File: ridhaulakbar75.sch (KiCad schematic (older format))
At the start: 184 parts, among them J1 SWD, J2 Ex_Bat, J3 Ex_USB, J4 RESET, J5 Underglow, Q1 AO3407, Q2 AO3407, SW1 Rotary_Encoder_Switch, U2 E73-2G4M08S1C-52840, U3 XC6220B331MR, U4 TP4054, Y1 32.768kHz

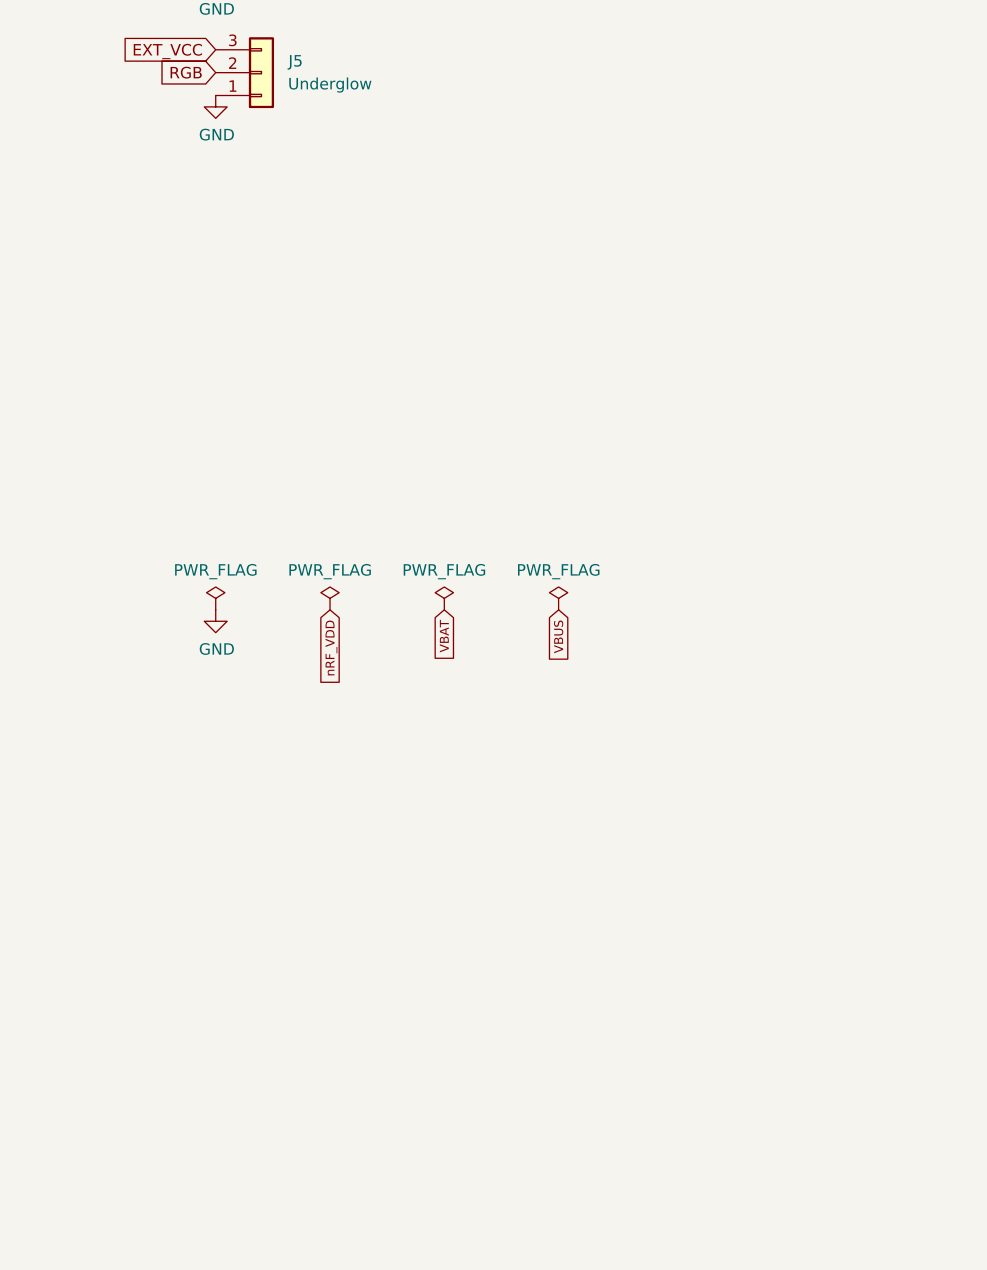
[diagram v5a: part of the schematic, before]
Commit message: add usb c back and add iso
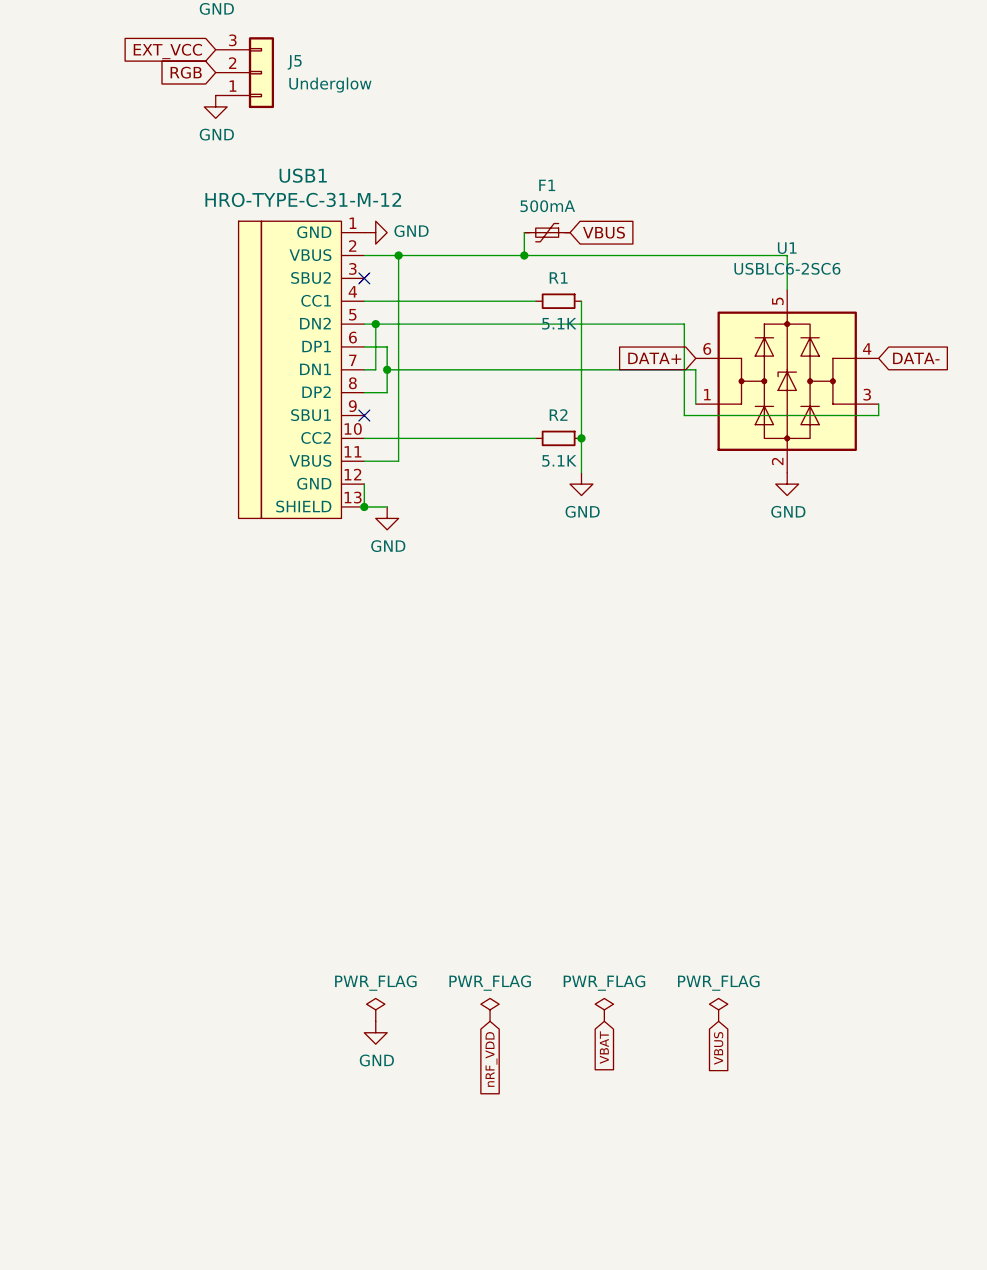
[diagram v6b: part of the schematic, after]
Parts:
- added F1: 500mA, Fuse:Fuse_1206_3216Metric, symbol Device:Polyfuse_Small
- added R1, R2: 5.1K, Resistor_SMD:R_0603_1608Metric, symbol Device:R_Small
- added U1: USBLC6-2SC6, Package_TO_SOT_SMD:SOT-23-6, symbol Power_Protection:USBLC6-2SC6
- added USB1: HRO-TYPE-C-31-M-12, Type-C:HRO-TYPE-C-31-M-12-HandSoldering, symbol keebio:HRO-TYPE-C-31-M-12
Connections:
- net DATA+: now also U1.6 (I/O1)
- net DATA-: now also U1.4 (I/O2)
- net GND: now also R1.1, R2.1, U1.2 (GND), USB1.1 (GND), USB1.12 (GND), USB1.13 (SHIELD)
- net VBUS: now also F1.1
- new net: R2.2, USB1.10 (CC2)
- new net: F1.2, U1.5 (VBUS), USB1.11 (VBUS), USB1.2 (VBUS)
- new net: R1.2, USB1.4 (CC1)
- new net: U1.3 (I/O2), USB1.5 (DN2), USB1.7 (DN1)
- new net: U1.1 (I/O1), USB1.6 (DP1), USB1.8 (DP2)
- no-connect marks 0 -> 2
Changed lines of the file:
@@
 L power:PWR_FLAG #FLG01
 U 1 1 60D8BBF8
-P 11250 7800
-F 0 "#FLG01" H 11250 7875 50  0001 C CNN
-F 1 "PWR_FLAG" H 11250 7973 50  0000 C CNN
-F 2 "" H 11250 7800 50  0001 C CNN
-F 3 "~" H 11250 7800 50  0001 C CNN
-	1    11250 7800
+P 11950 9600
+F 0 "#FLG01" H 11950 9675 50  0001 C CNN
+F 1 "PWR_FLAG" H 11950 9773 50  0000 C CNN
+F 2 "" H 11950 9600 50  0001 C CNN
+F 3 "~" H 11950 9600 50  0001 C CNN
+	1    11950 9600
 	1    0    0    -1
 $EndComp
@@
 L power:PWR_FLAG #FLG02
 U 1 1 60D8D705
-P 11750 7800
-F 0 "#FLG02" H 11750 7875 50  0001 C CNN
-F 1 "PWR_FLAG" H 11750 7973 50  0000 C CNN
-F 2 "" H 11750 7800 50  0001 C CNN
-F 3 "~" H 11750 7800 50  0001 C CNN
-	1    11750 7800
+P 12450 9600
+F 0 "#FLG02" H 12450 9675 50  0001 C CNN
+F 1 "PWR_FLAG" H 12450 9773 50  0000 C CNN
+F 2 "" H 12450 9600 50  0001 C CNN
+F 3 "~" H 12450 9600 50  0001 C CNN
+	1    12450 9600
 	1    0    0    -1
 $EndComp
@@
 L power:PWR_FLAG #FLG03
 U 1 1 60D8DA8A
-P 12250 7800
-F 0 "#FLG03" H 12250 7875 50  0001 C CNN
-F 1 "PWR_FLAG" H 12250 7973 50  0000 C CNN
-F 2 "" H 12250 7800 50  0001 C CNN
-F 3 "~" H 12250 7800 50  0001 C CNN
-	1    12250 7800
+P 12950 9600
+F 0 "#FLG03" H 12950 9675 50  0001 C CNN
+F 1 "PWR_FLAG" H 12950 9773 50  0000 C CNN
+F 2 "" H 12950 9600 50  0001 C CNN
+F 3 "~" H 12950 9600 50  0001 C CNN
+	1    12950 9600
 	1    0    0    -1
 $EndComp
@@
 L power:PWR_FLAG #FLG04
 U 1 1 60D8DE71
-P 12750 7800
-F 0 "#FLG04" H 12750 7875 50  0001 C CNN
-F 1 "PWR_FLAG" H 12750 7973 50  0000 C CNN
-F 2 "" H 12750 7800 50  0001 C CNN
-F 3 "~" H 12750 7800 50  0001 C CNN
-	1    12750 7800
+P 13450 9600
+F 0 "#FLG04" H 13450 9675 50  0001 C CNN
+F 1 "PWR_FLAG" H 13450 9773 50  0000 C CNN
+F 2 "" H 13450 9600 50  0001 C CNN
+F 3 "~" H 13450 9600 50  0001 C CNN
+	1    13450 9600
 	1    0    0    -1
 $EndComp
@@
 L power:GND #PWR07
 U 1 1 60D8F3D0
-P 11250 7800
-F 0 "#PWR07" H 11250 7550 50  0001 C CNN
-F 1 "GND" H 11255 7627 50  0000 C CNN
-F 2 "" H 11250 7800 50  0001 C CNN
-F 3 "" H 11250 7800 50  0001 C CNN
-	1    11250 7800
-	1    0    0    -1
-$EndComp
-Text GLabel 11750 7800 3    39   Input ~ 0
+P 11950 9600
+F 0 "#PWR07" H 11950 9350 50  0001 C CNN
+F 1 "GND" H 11955 9427 50  0000 C CNN
+F 2 "" H 11950 9600 50  0001 C CNN
+F 3 "" H 11950 9600 50  0001 C CNN
+	1    11950 9600
+	1    0    0    -1
+$EndComp
+Text GLabel 12450 9600 3    39   Input ~ 0
 nRF_VDD
-Text GLabel 12250 7800 3    39   Input ~ 0
+Text GLabel 12950 9600 3    39   Input ~ 0
 VBAT
-Text GLabel 12750 7800 3    39   Input ~ 0
+Text GLabel 13450 9600 3    39   Input ~ 0
 VBUS
 $Comp
@@
 Text GLabel 11250 5350 0    50   Input ~ 0
 EXT_VCC
+$Comp
+L keebio:HRO-TYPE-C-31-M-12 USB1
+U 1 1 605D3C2A
+P 11800 6700
+F 0 "USB1" H 11633 7497 60  0000 C CNN
+F 1 "HRO-TYPE-C-31-M-12" H 11633 7391 60  0000 C CNN
+F 2 "Type-C:HRO-TYPE-C-31-M-12-HandSoldering" H 11800 6700 60  0001 C CNN
+F 3 "" H 11800 6700 60  0001 C CNN
+	1    11800 6700
+	1    0    0    -1
+$EndComp
+$Comp
+L Device:Polyfuse_Small F1
+U 1 1 605D8FD4
+P 12700 6150
+F 0 "F1" V 12495 6150 50  0000 C CNN
+F 1 "500mA" V 12586 6150 50  0000 C CNN
+F 2 "Fuse:Fuse_1206_3216Metric" H 12750 5950 50  0001 L CNN
+F 3 "~" H 12700 6150 50  0001 C CNN
+	1    12700 6150
+	0    1    1    0
+$EndComp
+$Comp
+L Power_Protection:USBLC6-2SC6 U1
+U 1 1 605DD6E7
+P 13750 6800
+F 0 "U1" H 13750 7381 50  0000 C CNN
+F 1 "USBLC6-2SC6" H 13750 7290 50  0000 C CNN
+F 2 "Package_TO_SOT_SMD:SOT-23-6" H 13750 6300 50  0001 C CNN
+F 3 "https://www.st.com/resource/en/datasheet/usblc6-2.pdf" H 13950 7150 50  0001 C CNN
+	1    13750 6800
+	1    0    0    -1
+$EndComp
+$Comp
+L Device:R_Small R1
+U 1 1 605DED28
+P 12750 6450
+F 0 "R1" V 12650 6450 50  0000 C CNN
+F 1 "5.1K" V 12850 6450 50  0000 C CNN
+F 2 "Resistor_SMD:R_0603_1608Metric" H 12750 6450 50  0001 C CNN
+F 3 "~" H 12750 6450 50  0001 C CNN
+	1    12750 6450
+	0    1    1    0
+$EndComp
+NoConn ~ 11900 6950
+NoConn ~ 11900 6350
+Wire Wire Line
+	11900 7250 11900 7350
+Wire Wire Line
+	11900 7350 12000 7350
+Connection ~ 11900 7350
+$Comp
+L power:GND #PWR0103
+U 1 1 60636907
+P 12000 7350
+F 0 "#PWR0103" H 12000 7100 50  0001 C CNN
+F 1 "GND" H 12005 7177 50  0000 C CNN
+F 2 "" H 12000 7350 50  0001 C CNN
+F 3 "" H 12000 7350 50  0001 C CNN
+	1    12000 7350
+	1    0    0    -1
+$EndComp
+$Comp
+L power:GND #PWR0104
+U 1 1 60639607
+P 11900 6150
+F 0 "#PWR0104" H 11900 5900 50  0001 C CNN
+F 1 "GND" V 11905 6022 50  0000 R CNN
+F 2 "" H 11900 6150 50  0001 C CNN
+F 3 "" H 11900 6150 50  0001 C CNN
+	1    11900 6150
+	0    -1   -1   0
+$EndComp
+Wire Wire Line
+	13750 6250 13750 6400
+Wire Wire Line
+	12600 6250 13750 6250
+Text GLabel 12800 6150 2    50   Input ~ 0
+VBUS
+Wire Wire Line
+	12600 6150 12600 6250
+Wire Wire Line
+	11900 6250 12050 6250
+Connection ~ 12600 6250
+$Comp
+L Device:R_Small R2
+U 1 1 60678896
+P 12750 7050
+F 0 "R2" V 12650 7050 50  0000 C CNN
+F 1 "5.1K" V 12850 7050 50  0000 C CNN
+F 2 "Resistor_SMD:R_0603_1608Metric" H 12750 7050 50  0001 C CNN
+F 3 "~" H 12750 7050 50  0001 C CNN
+	1    12750 7050
+	0    1    1    0
+$EndComp
+Wire Wire Line
+	11900 6450 12650 6450
+Wire Wire Line
+	11900 7050 12650 7050
+Wire Wire Line
+	12850 6450 12850 7050
+Connection ~ 12850 7050
+Wire Wire Line
+	12850 7050 12850 7200
+$Comp
+L power:GND #PWR0105
+U 1 1 606CF4F1
+P 12850 7200
+F 0 "#PWR0105" H 12850 6950 50  0001 C CNN
+F 1 "GND" H 12855 7027 50  0000 C CNN
+F 2 "" H 12850 7200 50  0001 C CNN
+F 3 "" H 12850 7200 50  0001 C CNN
+	1    12850 7200
+	1    0    0    -1
+$EndComp
+Wire Wire Line
+	11900 6550 11950 6550
+Wire Wire Line
+	11950 6550 11950 6750
+Wire Wire Line
+	11950 6750 11900 6750
+Wire Wire Line
+	11900 6650 12000 6650
+Wire Wire Line
+	12000 6650 12000 6750
+Wire Wire Line
+	12000 6850 11900 6850
+Wire Wire Line
+	11900 7150 12050 7150
+Wire Wire Line
+	12050 7150 12050 6250
+Connection ~ 12050 6250
+Wire Wire Line
+	12050 6250 12600 6250
+$Comp
+L power:GND #PWR0106
+U 1 1 60727314
+P 13750 7200
+F 0 "#PWR0106" H 13750 6950 50  0001 C CNN
+F 1 "GND" H 13755 7027 50  0000 C CNN
+F 2 "" H 13750 7200 50  0001 C CNN
+F 3 "" H 13750 7200 50  0001 C CNN
+	1    13750 7200
+	1    0    0    -1
+$EndComp
+Wire Wire Line
+	12000 6750 13350 6750
+Wire Wire Line
+	13350 6750 13350 6900
+Connection ~ 12000 6750
+Wire Wire Line
+	12000 6750 12000 6850
+Wire Wire Line
+	11950 6550 13300 6550
+Wire Wire Line
+	13300 6550 13300 6950
+Wire Wire Line
+	13300 6950 14150 6950
+Wire Wire Line
+	14150 6950 14150 6900
+Connection ~ 11950 6550
+Text GLabel 14150 6700 2    50   Input ~ 0
+DATA-
+Text GLabel 13350 6700 0    50   Input ~ 0
+DATA+
 $EndSCHEMATC
